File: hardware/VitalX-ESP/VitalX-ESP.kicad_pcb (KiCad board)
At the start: 4 copper layers, 73 x 63 mm, 57 parts, among them J1 ECG Probe connector, J2 GSR Probe connector, J3 PROG, J4 JTAG, J5 Power terminal, Q1 BSS138, SW2 Reset, U1 AD8232ACPZ-R7, U3 ADP160AUJZ-1.8-R7, U4 ADPD144RI-ACEZ-RL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

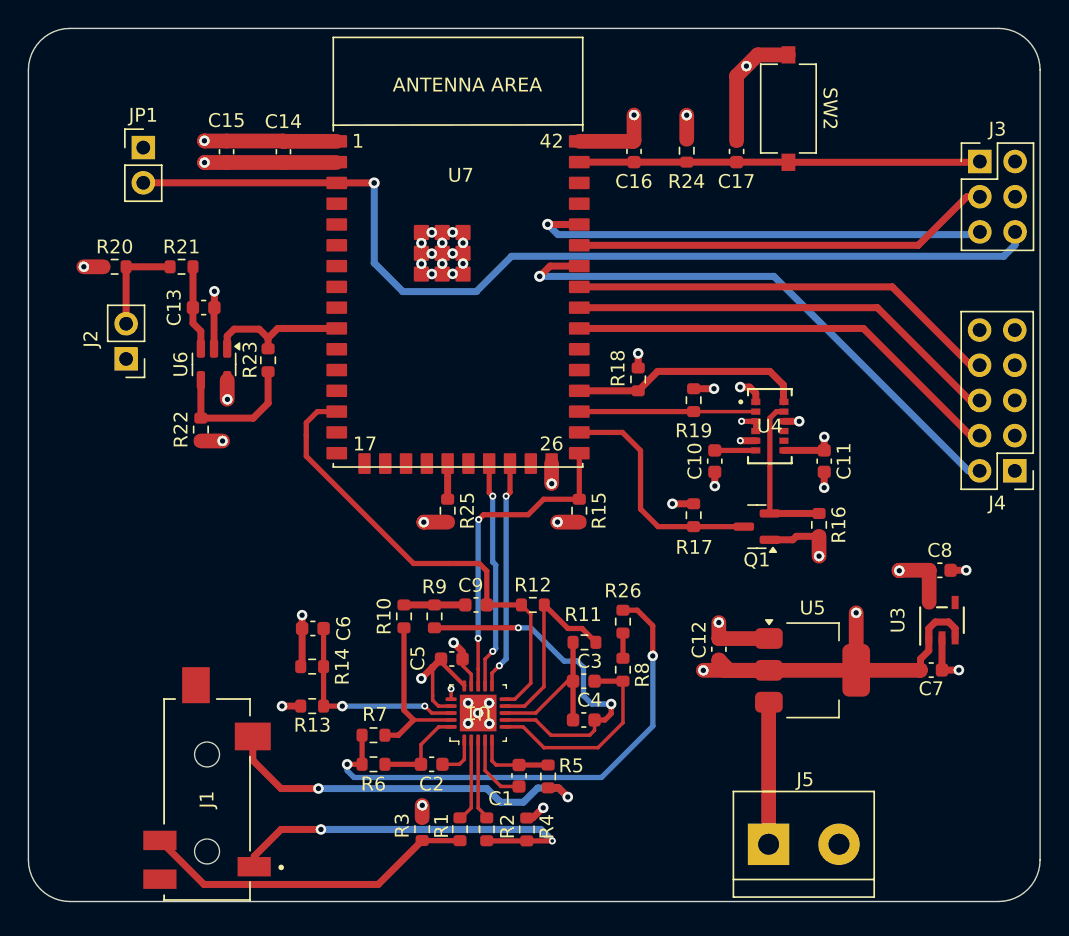
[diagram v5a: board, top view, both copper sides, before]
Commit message: [nightly] Finallize PCB
Seperate Antenna ground plane
Add grounded mounting hole
Add logo
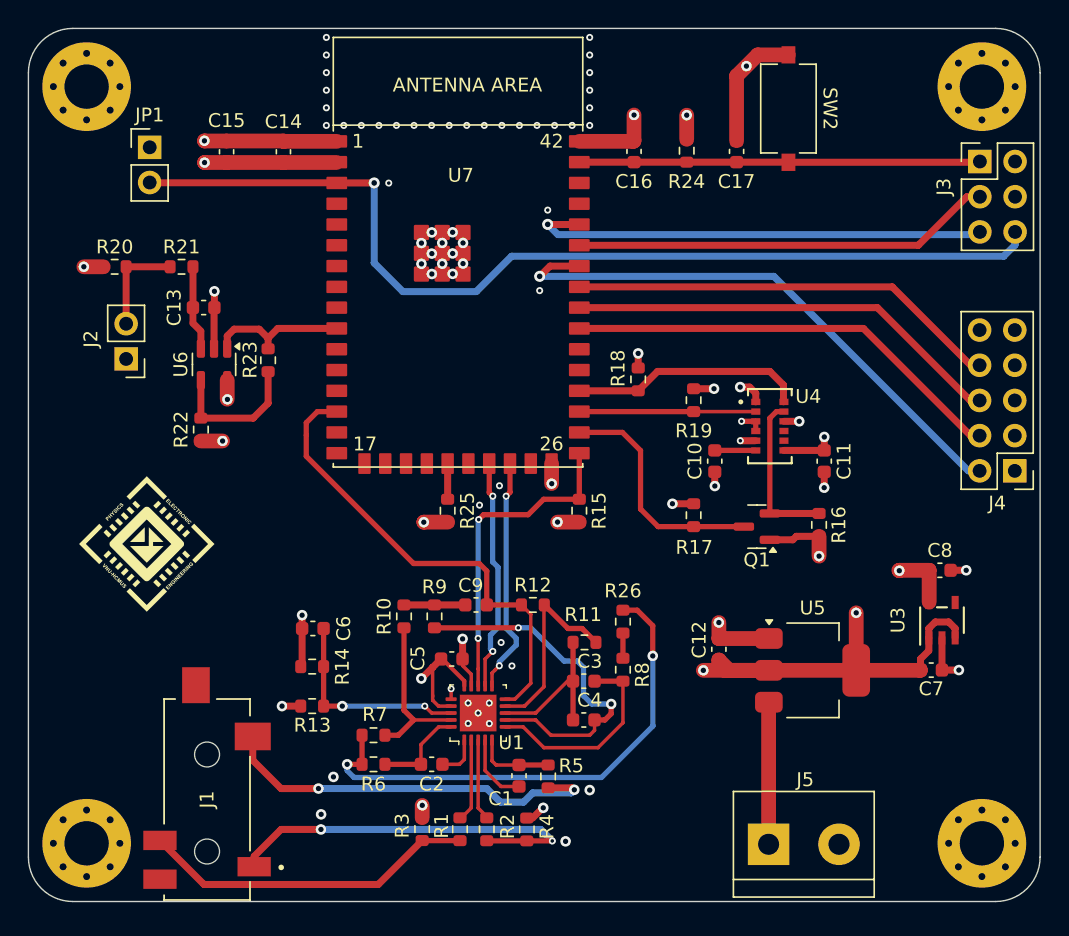
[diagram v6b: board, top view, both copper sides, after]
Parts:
- added G***: LOGO, Local-LIB:dpee-logo-10x10, F.Cu at (110.5, 84.2)
- added H1: M3, MountingHole:MountingHole_3.2mm_M3_Pad_Via, F.Cu at (106.2, 51.2)
- added H2: M3, MountingHole:MountingHole_3.2mm_M3_Pad_Via, F.Cu at (170.8, 51.2)
- added H3: M3, MountingHole:MountingHole_3.2mm_M3_Pad_Via, F.Cu at (170.8, 105.8)
- added H4: M3, MountingHole:MountingHole_3.2mm_M3_Pad_Via, F.Cu at (106.2, 105.8)
- moved JP1 0.46 mm to (110.8, 55.6)
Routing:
- net /LOD-: track 16.6 -> 17.2 mm
- net GND: vias 34 -> 71
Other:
- outline, holes or cut-outs redrawn

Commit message: Update for fabrication: Add top&bot layer mass, change logo, add GND vias, refine text
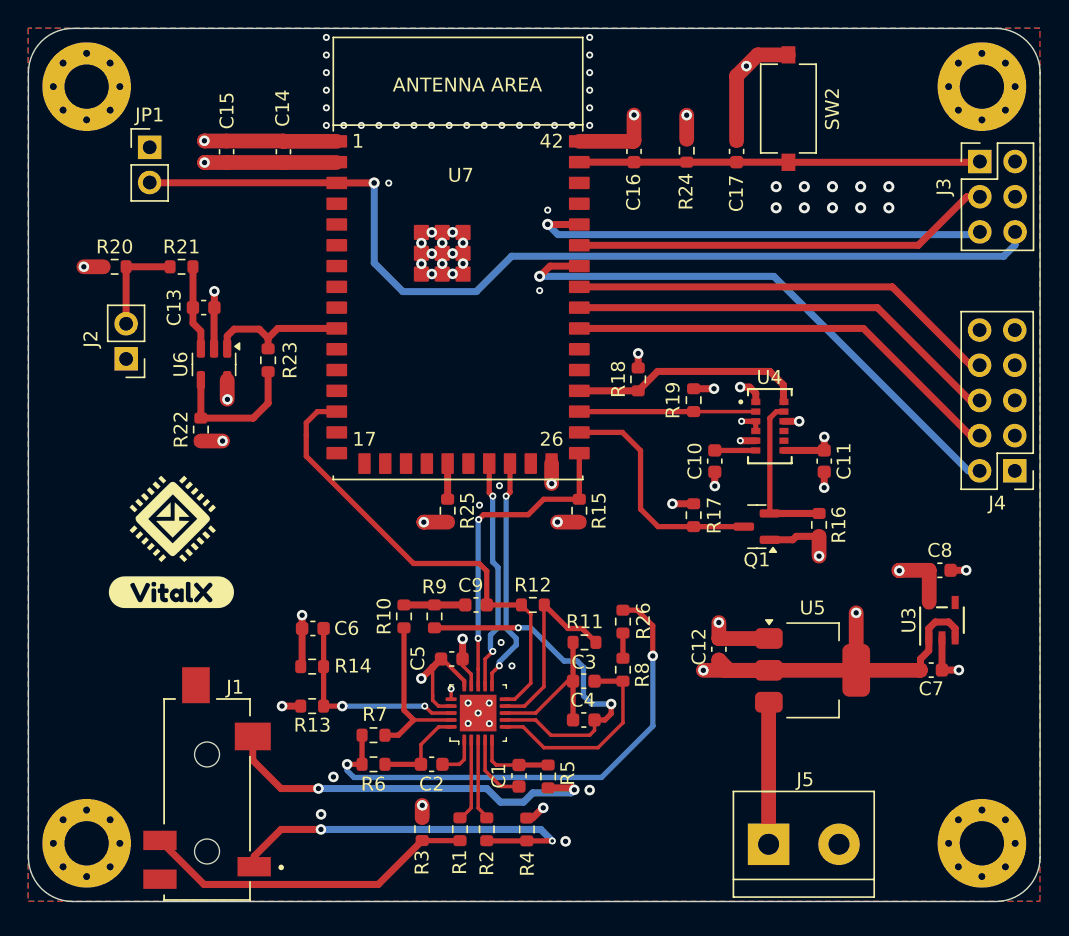
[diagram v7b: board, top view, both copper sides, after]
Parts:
- removed the G*** at (110.5, 84.2)
- added G***: LOGO, dpee-logo:dpee-logo_5x5, F.Cu at (112.4, 82.4)
- added kibuzzard-673C1CE7: G***, kibuzzard-673C1CE7, F.Cu at (112.3, 87.7)
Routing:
- net GND: vias 71 -> 81
- added copper zone on B.Cu, net GND
- added copper zone on F.Cu, net GND
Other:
- board text added: "Prototype Version Sample A0"
